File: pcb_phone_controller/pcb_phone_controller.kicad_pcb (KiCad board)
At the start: 2 copper layers, 115.3 x 51.7 mm, 38 parts, among them SW17 SS-12D00-G 4 E, X1 KAILH-MINI-SILENT-SWITCH, Y1 KAILH-MINI-SILENT-SWITCH

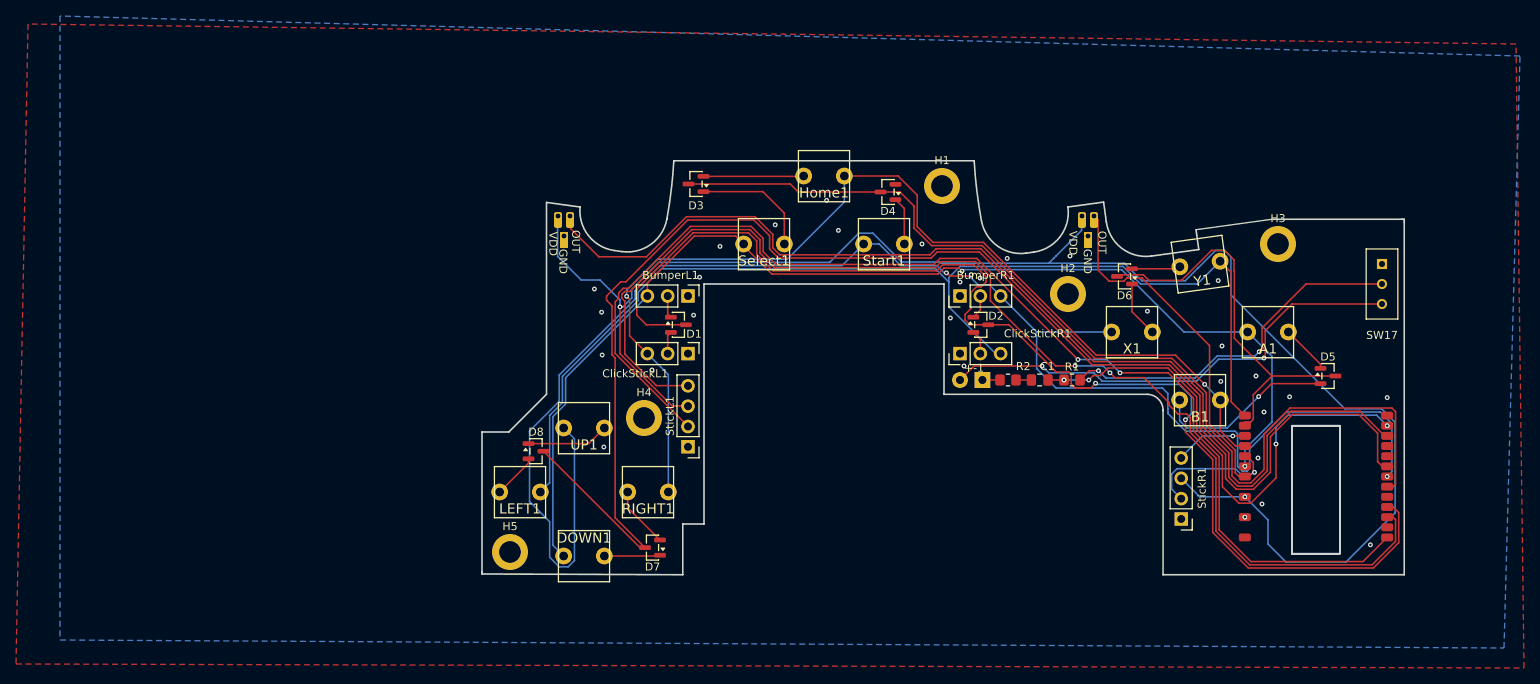
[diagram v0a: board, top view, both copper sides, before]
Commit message: PCB cleanup (libs and traces)
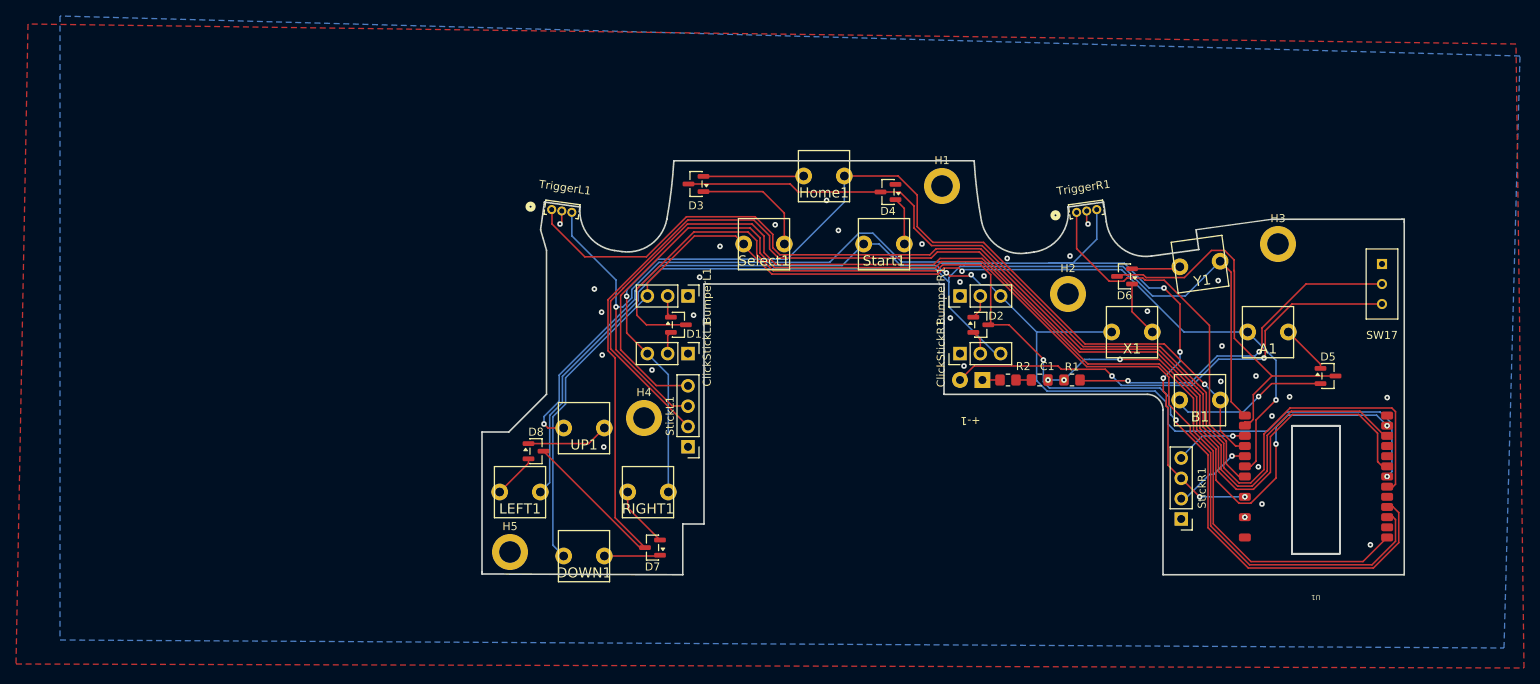
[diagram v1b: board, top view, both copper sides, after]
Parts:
- +-1: footprint CC-Library:Battery_connection -> Lib_controller:Battery_connection
- A1, B1, DOWN1, Home1, LEFT1, RIGHT1, Select1, Start1, UP1, X1, Y1: footprint CC-Library:KAILH-MINI-SILENT-SWITCH -> Lib_controller:KAILH-MINI-SILENT-SWITCH
- BumperL1, BumperR1, ClickStickL1, ClickStickR1: footprint CC-Library:PinHeader_1x03_P2.54mm_Vertical -> Lib_controller:PinHeader_1x03_P2.54mm_Vertical
- SW17: footprint CC-Library:1P2T_SS-12D00_CNK -> Lib_controller:1P2T_SS-12D00_CNK
- TriggerL1, TriggerR1: footprint CC-Library:SEN3_SS49E_HNW -> Lib_controller:ss49e
- U1: footprint CC-Library:Seeed Studio XIAO ESP32S3 Plus -> Lib_controller:Seeed Studio XIAO ESP32S3 Plus
- moved TriggerR1 3.09 mm to (182.5, 98.9), turned to 7.853 degrees
- moved TriggerL1 3.06 mm to (117.6, 98.9), turned to -7.853 degrees
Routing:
- net +3.3V: track 204.5 -> 154.4 mm, vias 2 -> 6
- net Column 2: track 197.9 -> 153.8 mm, vias 3 -> 4
- net Net-(StickR1-Y): track 17.2 -> 10.7 mm
- net Row 0: track 151.2 -> 146.4 mm
- net Net-(TriggerL1-OUT): track 134.7 -> 137.7 mm
- net Net-(B1-Pad1): track 22.9 -> 20.0 mm
- net GND: track 0.00 -> 2.88 mm, vias 30 -> 32
- net Net-(TriggerR1-OUT): track 43.8 -> 46.7 mm
- net Column 3: track 140.5 -> 141.7 mm
- net Net-(StickL1-Y): track 148.1 -> 149.1 mm, vias 2 -> 0
- net Net-(C1-Pad1): track 63.5 -> 64.4 mm, vias 4 -> 5
- net Column 0: track 142.4 -> 143.2 mm
- net Row 3: track 183.6 -> 183.1 mm
- net Net-(StickL1-X): track 149.7 -> 149.5 mm, vias 2 -> 0
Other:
- outline, holes or cut-outs redrawn

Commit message: PCB shape and reroute to make space for sticks
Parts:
- moved StickL1 16.2 mm to (120.5, 120.6)
- moved U1 3.10 mm to (211.5, 149.8)
- moved StickR1 2.53 mm to (197.0, 140.8)
- moved Y1 0.16 mm to (197.0, 108.2)
- moved X1 0.15 mm to (188.5, 116.6)
- moved DOWN1 0.15 mm to (120.0, 144.6)
- moved LEFT1 0.15 mm to (112.0, 136.6)
- moved RIGHT1 0.15 mm to (128.0, 136.6)
- moved UP1 0.15 mm to (120.0, 128.6)
- moved A1 0.14 mm to (205.5, 116.6)
- moved B1 0.13 mm to (197.0, 125.1)
- moved Home1 0.09 mm to (150.0, 97.1)
- moved Select1 0.09 mm to (142.5, 105.6)
- moved Start1 0.09 mm to (157.5, 105.6)
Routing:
- net Net-(StickL1-X): track 149.5 -> 130.9 mm, vias 0 -> 3
- net Row 1: track 126.6 -> 112.7 mm, vias 0 -> 2
- net Net-(C1-Pad1): track 64.4 -> 51.7 mm
- net +3.3V: track 154.4 -> 142.9 mm, vias 6 -> 3
- net Row 0: track 146.4 -> 135.7 mm, vias 2 -> 4
- net Row 3: track 183.1 -> 172.9 mm, vias 0 -> 2
- net Net-(StickL1-Y): track 149.1 -> 139.0 mm, vias 0 -> 3
- net Net-(TriggerL1-OUT): track 137.7 -> 127.9 mm, vias 0 -> 2
- net Column 1: track 131.0 -> 135.8 mm
- net Column 3: track 141.7 -> 145.7 mm
- net Net-(StickR1-Y): track 10.7 -> 6.91 mm
- net Column 0: track 143.2 -> 146.6 mm
- net Row 2: track 49.2 -> 52.6 mm
- net Column 2: track 153.8 -> 150.4 mm
- net Net-(StickR1-X): track 9.14 -> 5.86 mm
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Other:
- board size 115.3 x 51.7 mm -> 115.3 x 53.2 mm
